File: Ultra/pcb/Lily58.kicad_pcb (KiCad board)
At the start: 2 copper layers, 142.5 x 106.3 mm, 124 parts, among them J1 4PIN, P1 i2c_pin, P2 i2c_pin, P3 ICSP, P4 OLED, SW1 SW_PUSH, SW10 SW_PUSH, SW11 SW_PUSH, SW12 SW_PUSH, SW13 SW_PUSH, SW14 SW_PUSH, SW15 SW_PUSH, SW16 SW_PUSH, SW17 SW_PUSH, SW18 SW_PUSH, SW19 SW_PUSH, SW2 SW_PUSH, SW20 SW_PUSH, SW21 SW_PUSH, SW22 SW_PUSH, SW23 SW_PUSH, SW24 SW_PUSH, SW25 SW_PUSH, SW26 SW_PUSH, SW27 SW_PUSH, SW28 SW_PUSH, SW29 SW_PUSH, SW3 SW_PUSH, SW30 RotaryEncoder_Switch, SW4 SW_PUSH, SW5 SW_PUSH, SW6 SW_PUSH, SW7 SW_PUSH, SW8 SW_PUSH, SW9 SW_PUSH, U1 ProMicro

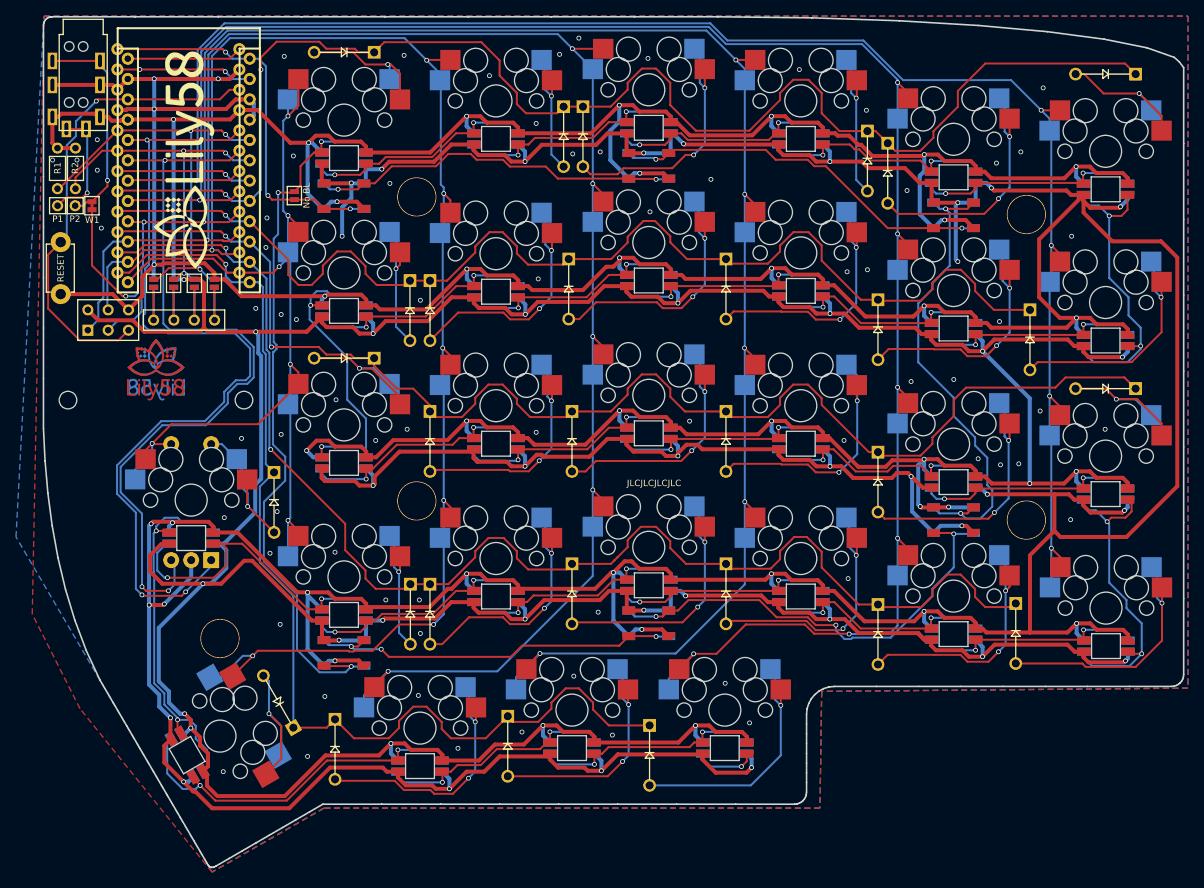
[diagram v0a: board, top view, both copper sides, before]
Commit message: Clean up triangle above bottom thumb key
Cases have trouble covering this, so keep it as bare as possible.
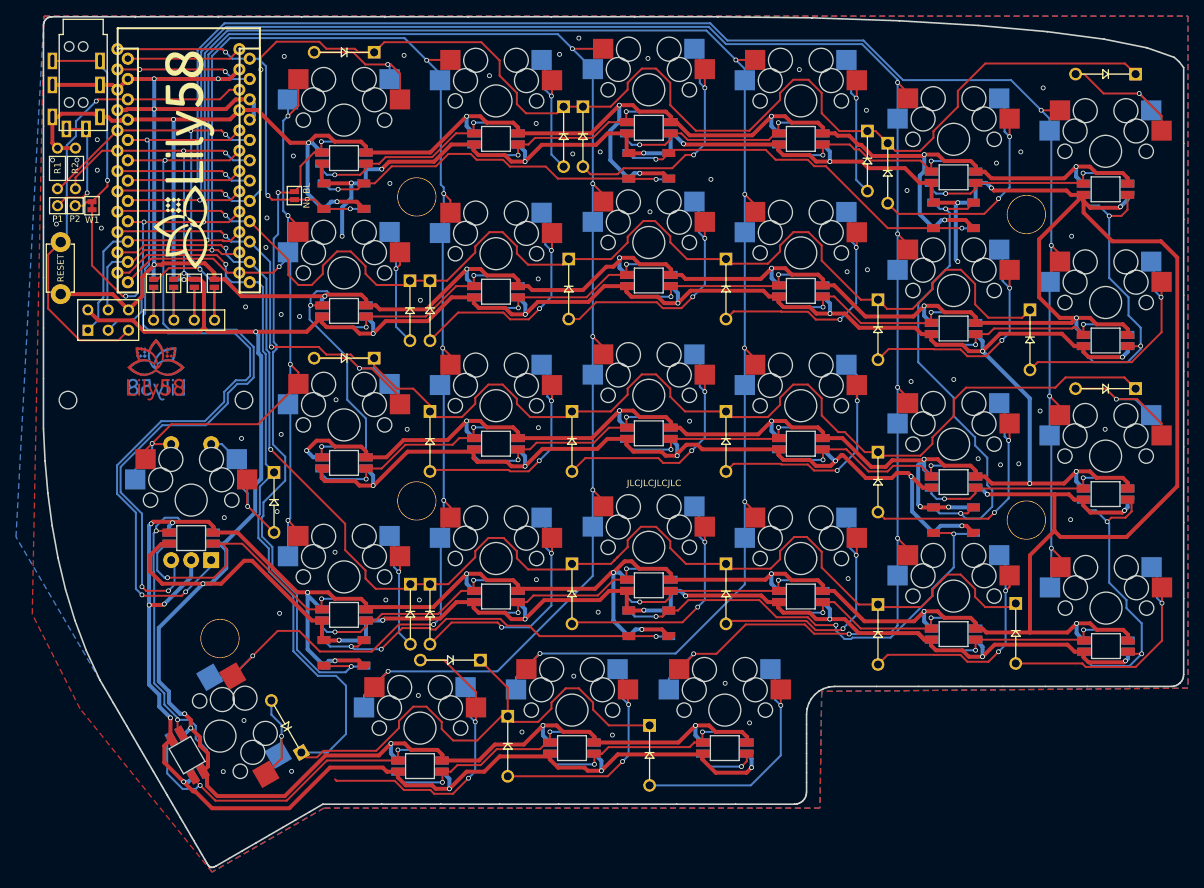
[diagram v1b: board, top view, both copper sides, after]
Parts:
- moved D27 18.2 mm to (133.8, 117.5), turned to 0 degrees
- moved D26 3.26 mm to (113.3, 125.8)
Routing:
- net row4: track 136.1 -> 155.1 mm
- net Net-(D27-Pad2): track 32.3 -> 42.8 mm
- net Net-(D26-Pad2): track 20.0 -> 13.1 mm
- net row1: track 145.7 -> 148.4 mm
- net col4: track 194.6 -> 196.4 mm
- net Net-(D33-Pad4): track 47.0 -> 48.1 mm
- net row2: track 166.3 -> 167.1 mm
- net Net-(LED11-Pad4): track 29.2 -> 29.9 mm
- net GND: track 940.5 -> 939.9 mm, vias 117 -> 113

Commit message: Minor routing tweaks
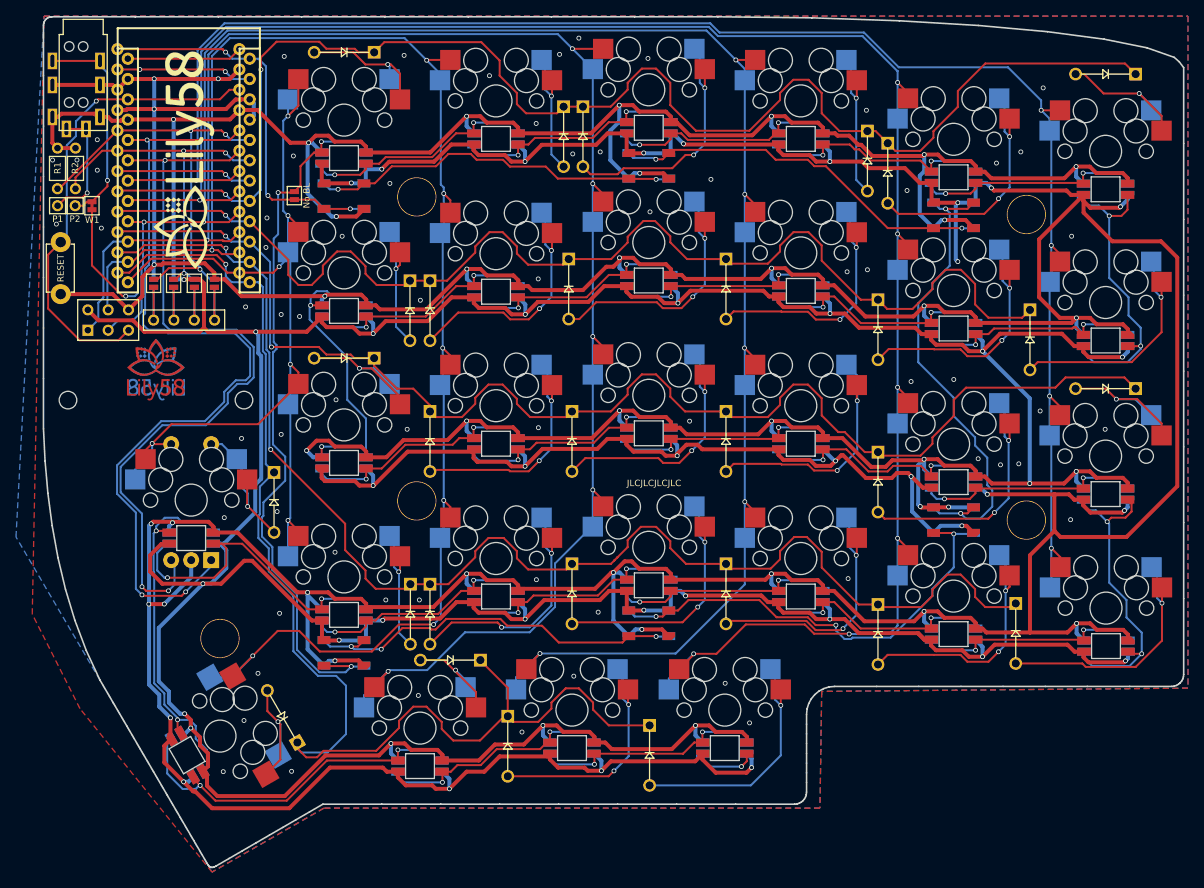
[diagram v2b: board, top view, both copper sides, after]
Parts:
- moved D26 1.35 mm to (112.8, 124.5)
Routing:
- net Net-(D27-Pad2): track 42.8 -> 13.2 mm, vias 2 -> 1
- net GND: track 939.9 -> 932.8 mm, vias 113 -> 112
- net Net-(D26-Pad2): track 13.1 -> 16.4 mm
- net row4: track 155.1 -> 158.0 mm
- net VCC: track 889.9 -> 890.7 mm
- net col0: track 213.2 -> 213.9 mm
- net Net-(D33-Pad4): track 48.1 -> 48.8 mm
- net col1: track 238.9 -> 239.5 mm
